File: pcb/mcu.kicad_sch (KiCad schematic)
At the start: 29 parts, among them SW3 TS04-66-50-BK-160-SMT, SW4 PTS645VH58-2 LFS, U1 W25Q128JVS, U2 RP2040, Y1 ABM8AIG-12.000MHZ-12-2Z-T3

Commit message: Change power switch
- Replace push button with rocker
- Added some notches to outside of PCB for aligning with enclosure
- Upgrade to KiCAD 9.0
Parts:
- U1: footprint Package_SO:SOIC-8_5.275x5.275mm_P1.27mm -> Package_SO:SOIC-8_5.23x5.23mm_P1.27mm
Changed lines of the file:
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@@
 (kicad_sch
-	(version 20231120)
+	(version 20241209)
 	(generator "eeschema")
-	(generator_version "8.0")
+	(generator_version "9.0")
 	(paper "A4")
 	(title_block
@@
 		(members "SDI" "~{CS0}" "SCK" "~{LDAC}")
 	)
+	(arc
+		(start 77.47 166.37)
+		(mid 76.0505 166.0344)
+		(end 74.93 165.1)
+		(stroke
+			(width 0)
+			(type default)
+		)
+		(fill
+			(type none)
+		)
+	)
+	(text "NB: Place 1uF\nclose to pin 45"
+		(exclude_from_sim no)
+		(at 101.346 29.718 0)
+		(effects
+			(font
+				(size 1.27 1.27)
+			)
+			(justify left)
+		)
+	)
+	(text "Table 2 from Section 1.4.3. GPIO Functions, page 13"
+		(exclude_from_sim no)
+		(at 237.49 149.86 0)
+		(effects
+			(font
+				(size 1.27 1.27)
+			)
+		)
+	)
+	(text "PIO1"
+		(exclude_from_sim no)
+		(at 176.276 111.506 0)
+		(effects
+			(font
+				(size 1.27 1.27)
+			)
+			(justify left bottom)
+		)
+	)
+	(text "NB: Place 1uF\nclose to pin 44"
+		(exclude_from_sim no)
+		(at 226.06 37.084 0)
+		(effects
+			(font
+				(size 1.27 1.27)
+			)
+			(justify left)
+		)
+	)
+	(text "PIO0"
+		(exclude_from_sim no)
+		(at 192.024 74.676 0)
+		(effects
+			(font
+				(size 1.27 1.27)
+			)
+			(justify left bottom)
+		)
+	)
+	(text "SPI1"
+		(exclude_from_sim no)
+		(at 191.77 118.11 0)
+		(effects
+			(font
+				(size 1.27 1.27)
+			)
+			(justify left bottom)
+		)
+	)
+	(text "RP2040 hardware design guide:\nhttps://datasheets.raspberrypi.com/rp2040/hardware-design-with-rp2040.pdf\n"
+		(exclude_from_sim no)
+		(at 17.272 192.278 0)
+		(effects
+			(font
+				(size 1.27 1.27)
+			)
+			(justify left)
+		)
+	)
+	(text "~{BOOT_SEL}"
+		(exclude_from_sim no)
+		(at 77.978 167.64 0)
+		(effects
+			(font
+				(size 1.27 1.27)
+			)
+			(justify left bottom)
+		)
+	)
+	(text "NB: Place resistors\nclose to pins 46 & 47"
+		(exclude_from_sim no)
+		(at 102.108 62.23 0)
+		(effects
+			(font
+				(size 1.27 1.27)
+			)
+			(justify right bottom)
+		)
+	)
 	(junction
 		(at 199.39 33.02)
@@
 		)
 	)
-	(arc
-		(start 77.47 166.37)
-		(mid 76.0505 166.0344)
-		(end 74.93 165.1)
-		(stroke
-			(width 0)
-			(type default)
-		)
-		(fill
-			(type none)
-		)
-	)
 	(image
 		(at 241.808 88.9)
@@
 		)
 	)
-	(text "NB: Place 1uF\nclose to pin 45"
-		(exclude_from_sim no)
-		(at 101.346 29.718 0)
-		(effects
-			(font
-				(size 1.27 1.27)
-			)
-			(justify left)
-		)
-	)
-	(text "Table 2 from Section 1.4.3. GPIO Functions, page 13"
-		(exclude_from_sim no)
-		(at 237.49 149.86 0)
-		(effects
-			(font
-				(size 1.27 1.27)
-			)
-		)
-	)
-	(text "PIO1"
-		(exclude_from_sim no)
-		(at 176.276 111.506 0)
-		(effects
-			(font
-				(size 1.27 1.27)
-			)
-			(justify left bottom)
-		)
-	)
-	(text "NB: Place 1uF\nclose to pin 44"
-		(exclude_from_sim no)
-		(at 226.06 37.084 0)
-		(effects
-			(font
-				(size 1.27 1.27)
-			)
-			(justify left)
-		)
-	)
-	(text "PIO0"
-		(exclude_from_sim no)
-		(at 192.024 74.676 0)
-		(effects
-			(font
-				(size 1.27 1.27)
-			)
-			(justify left bottom)
-		)
-	)
-	(text "SPI1"
-		(exclude_from_sim no)
-		(at 191.77 118.11 0)
-		(effects
-			(font
-				(size 1.27 1.27)
-			)
-			(justify left bottom)
-		)
-	)
-	(text "RP2040 hardware design guide:\nhttps://datasheets.raspberrypi.com/rp2040/hardware-design-with-rp2040.pdf\n"
-		(exclude_from_sim no)
-		(at 17.272 192.278 0)
-		(effects
-			(font
-				(size 1.27 1.27)
-			)
-			(justify left)
-		)
-	)
-	(text "~{BOOT_SEL}"
-		(exclude_from_sim no)
-		(at 77.978 167.64 0)
-		(effects
-			(font
-				(size 1.27 1.27)
-			)
-			(justify left bottom)
-		)
-	)
-	(text "NB: Place resistors\nclose to pins 46 & 47"
-		(exclude_from_sim no)
-		(at 102.108 62.23 0)
-		(effects
-			(font
-				(size 1.27 1.27)
-			)
-			(justify right bottom)
-		)
-	)
 	(label "~{RES}"
 		(at 175.26 119.38 0)
-		(fields_autoplaced yes)
 		(effects
 			(font
@@
 	(label "QSPI_{D0}"
 		(at 62.23 154.94 0)
-		(fields_autoplaced yes)
 		(effects
 			(font
@@
 	(label "QSPI_{D2}"
 		(at 114.3 83.82 180)
-		(fields_autoplaced yes)
 		(effects
 			(font
@@
 	(label "QSPI_{D0}"
 		(at 114.3 78.74 180)
-		(fields_autoplaced yes)
 		(effects
 			(font
@@
 	(label "SCLK"
 		(at 175.26 124.46 0)
-		(fields_autoplaced yes)
 		(effects
 			(font
@@
 	(label "QSPI_{D1}"
 		(at 114.3 81.28 180)
-		(fields_autoplaced yes)
 		(effects
 			(font
@@
 	(label "QSPI_{CLK}"
 		(at 114.3 88.9 180)
-		(fields_autoplaced yes)
 		(effects
 			(font
@@
 	(label "QSPI_{CLK}"
 		(at 62.23 152.4 0)
-		(fields_autoplaced yes)
 		(effects
 			(font
@@
 	(label "QSPI_{D3}"
 		(at 62.23 162.56 0)
-		(fields_autoplaced yes)
 		(effects
 			(font
@@
 	(label "SDI"
 		(at 175.26 73.66 0)
-		(fields_autoplaced yes)
 		(effects
 			(font
@@
 	(label "QSPI_{D3}"
 		(at 114.3 86.36 180)
-		(fields_autoplaced yes)
 		(effects
 			(font
@@
 	(label "SCK"
 		(at 175.26 81.28 0)
-		(fields_autoplaced yes)
 		(effects
 			(font
@@
 	(label "~{CS1}"
 		(at 175.26 132.08 0)
-		(fields_autoplaced yes)
 		(effects
 			(font
@@
 	(label "~{LDAC}"
 		(at 175.26 83.82 0)
-		(fields_autoplaced yes)
 		(effects
 			(font
@@
 	(label "MOSI"
 		(at 175.26 127 0)
-		(fields_autoplaced yes)
 		(effects
 			(font
@@
 	(label "QSPI_{~{CS}}"
 		(at 114.3 73.66 180)
-		(fields_autoplaced yes)
 		(effects
 			(font
@@
 	(label "~{D{slash}C}"
 		(at 175.26 116.84 0)
-		(fields_autoplaced yes)
 		(effects
 			(font
@@
 	(label "QSPI_{D2}"
 		(at 62.23 160.02 0)
-		(fields_autoplaced yes)
 		(effects
 			(font
@@
 	(label "~{CS0}"
 		(at 175.26 78.74 0)
-		(fields_autoplaced yes)
 		(effects
 			(font
@@
 	(label "QSPI_{D1}"
 		(at 62.23 157.48 0)
-		(fields_autoplaced yes)
 		(effects
 			(font
@@
 	(label "QSPI_{~{CS}}"
 		(at 62.23 149.86 0)
-		(fields_autoplaced yes)
 		(effects
 			(font
@@
 		(shape output)
 		(at 190.5 114.3 0)
-		(fields_autoplaced yes)
 		(effects
 			(font
@@
 		(shape input)
 		(at 165.1 66.04 0)
-		(fields_autoplaced yes)
 		(effects
 			(font
@@
 		(shape input)
 		(at 165.1 109.22 0)
-		(fields_autoplaced yes)
 		(effects
 			(font
@@
 		(shape bidirectional)
 		(at 165.1 63.5 0)
-		(fields_autoplaced yes)
 		(effects
 			(font
@@
 		(shape bidirectional)
 		(at 91.44 66.04 180)
-		(fields_autoplaced yes)
 		(effects
 			(font
@@
 		(shape input)
 		(at 190.5 58.42 0)
-		(fields_autoplaced yes)
 		(effects
 			(font
@@
 		(shape bidirectional)
 		(at 104.14 124.46 180)
-		(fields_autoplaced yes)
 		(effects
 			(font
@@
 		(shape bidirectional)
 		(at 165.1 60.96 0)
-		(fields_autoplaced yes)
 		(effects
 			(font
@@
 		(shape input)
 		(at 165.1 111.76 0)
-		(fields_autoplaced yes)
 		(effects
 			(font
@@
 		(shape input)
 		(at 104.14 121.92 180)
-		(fields_autoplaced yes)
 		(effects
 			(font
@@
 		(shape bidirectional)
 		(at 91.44 63.5 180)
-		(fields_autoplaced yes)
 		(effects
 			(font
@@
 		(shape input)
 		(at 165.1 114.3 0)
-		(fields_autoplaced yes)
 		(effects
 			(font
@@
 		(shape output)
 		(at 190.5 71.12 0)
-		(fields_autoplaced yes)
 		(effects
 			(font
@@
 		(shape output)
 		(at 165.1 104.14 0)
-		(fields_autoplaced yes)
 		(effects
 			(font
@@
 		(shape output)
 		(at 165.1 96.52 0)
-		(fields_autoplaced yes)
 		(effects
 			(font
@@
 		(shape output)
 		(at 165.1 93.98 0)
-		(fields_autoplaced yes)
 		(effects
 			(font
@@
 		(shape output)
 		(at 190.5 55.88 0)
-		(fields_autoplaced yes)
 		(effects
 			(font
@@
 			)
 		)
-		(property "Footprint" "Package_SO:SOIC-8_5.275x5.275mm_P1.27mm"
+		(property "Footprint" "Package_SO:SOIC-8_5.23x5.23mm_P1.27mm"
 			(at 52.07 157.48 0)
 			(effects
@@
 			)
 		)
-		(property "Datasheet" "http://www.winbond.com/resource-files/w25q128jv_dtr%20revc%2003272018%20plus.pdf"
+		(property "Datasheet" "https://www.winbond.com/resource-files/w25q128jv_dtr%20revc%2003272018%20plus.pdf"
 			(at 52.07 157.48 0)
 			(effects

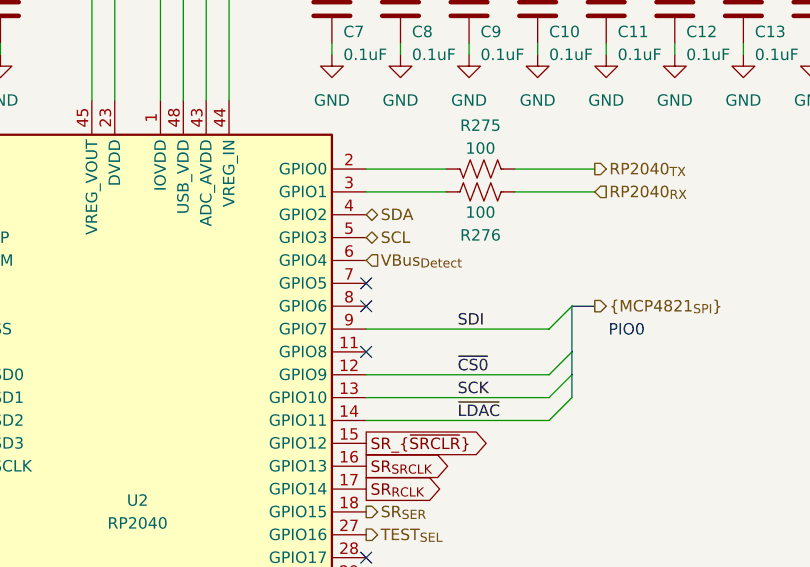
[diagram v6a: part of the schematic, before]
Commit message: Added module detect signal
- 100k pullup to VCC next to i2c bus that can be pulled down by module
  to assert its presence
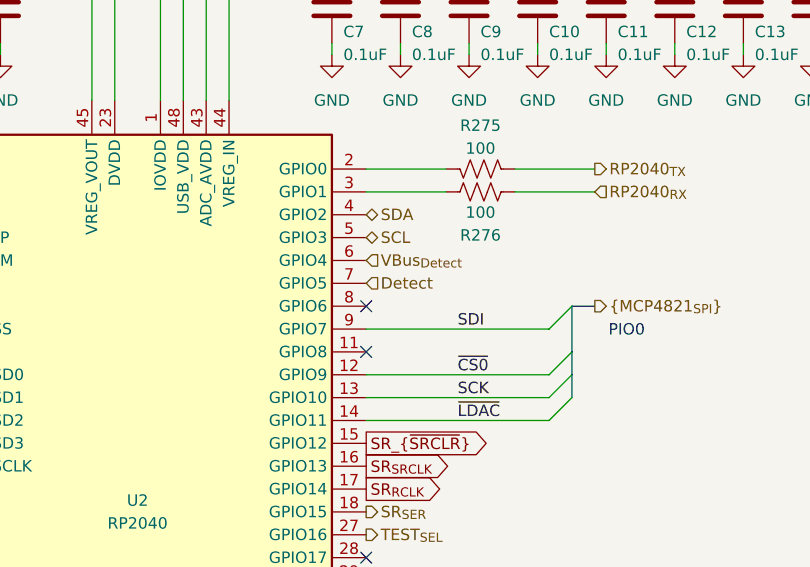
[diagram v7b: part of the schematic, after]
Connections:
- net Detect: now reaches U2.7 (GPIO5)
- no-connect marks 7 -> 6
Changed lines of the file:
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@@
 	(title_block
 		(title "Extracellular Electrophysiology Test Board")
-		(rev "B")
+		(rev "C")
 		(company "Open Ephys, Inc")
 		(comment 1 "Jonathan P. Newman")
@@
 	)
 	(no_connect
-		(at 165.1 68.58)
-	)
-	(no_connect
 		(at 165.1 129.54)
 	)
@@
 		)
 	)
+	(hierarchical_label "Detect"
+		(shape input)
+		(at 165.1 68.58 0)
+		(effects
+			(font
+				(size 1.27 1.27)
+			)
+			(justify left)
+		)
+	)

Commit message: Move SW4 closer to PCB edge
- Also, correct its footprint to 5.8mm actuator length rather than 8.3
which did not match its part number
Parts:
- SW4: footprint Button_Switch_THT:SW_Tactile_SPST_Angled_PTS645Vx83-2LFS -> Button_Switch_THT:SW_Tactile_SPST_Angled_PTS645Vx58-2LFS
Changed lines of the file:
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@@
 			)
 		)
-		(property "Footprint" "Button_Switch_THT:SW_Tactile_SPST_Angled_PTS645Vx83-2LFS"
+		(property "Footprint" "Button_Switch_THT:SW_Tactile_SPST_Angled_PTS645Vx58-2LFS"
 			(at 68.58 68.58 0)
 			(effects
